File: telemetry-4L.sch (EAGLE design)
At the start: 70 parts, among them SW1 MF-SW-TACT-4.2MM, SW2 PCM12SMTR, U1 ATSAMD21G18A-MUT, U2 SPX3819M5-L-3-0, U3 MCP73831T-2ACI/OT, U4 IRLML6344TRPBF, U5 SIM868, U6 BMP280, U7 MPU-9250, U8 TPS61253YFFR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

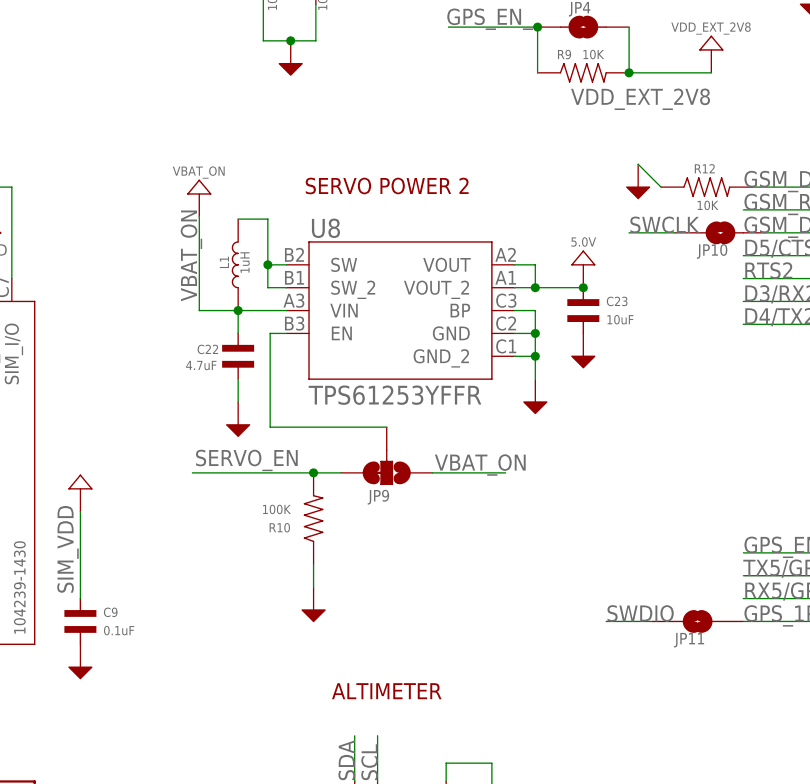
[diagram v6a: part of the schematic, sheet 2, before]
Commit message: Killed "Servo Power 2" components
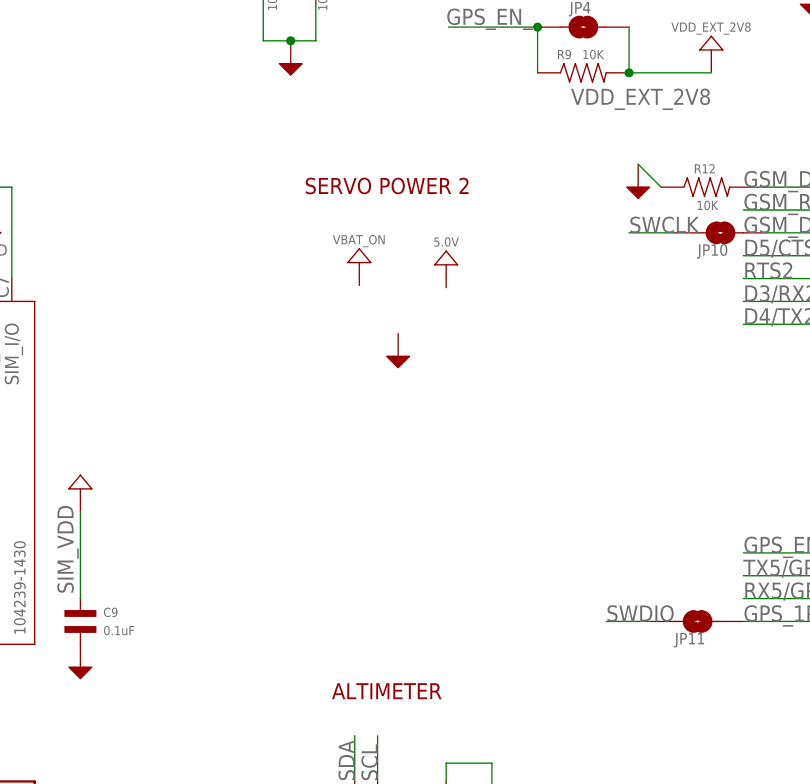
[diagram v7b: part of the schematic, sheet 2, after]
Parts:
- removed C22: 4.7uF, MF_Passives:CAPACITOR_NP_0402
- removed C23: 10uF, MF_Passives:CAPACITOR_NP_0603
- removed JP9: JUMPER-PAD-3-2OF3_NC_BY_TRACE_SMALL, SparkFun-Passives:JUMPER-PAD-3-2OF3_NC_BY_TRACE_SMALL
- removed L1: 1uH, MF_Passives:INDUCTOR_1210
- removed R10: 100K, MF_Passives:RESISTOR_0402
- removed U8: TPS61253YFFR, Custom:TPS61253YFFT
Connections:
- removed net 5VSW: L1.P$2, U8.SW, U8.SW_2
- removed net 5V_EN: JP9.2, U8.EN
- net 5.0V: no longer C23.P$1, U8.VOUT, U8.VOUT_2
- net GND: no longer C22.P$2, C23.P$2, R10.P$1, U8.BP, U8.GND, U8.GND_2
- net SERVO_EN: no longer JP9.3, R10.P$2
- net VBAT_ON: no longer C22.P$1, JP9.1, L1.P$1, U8.VIN
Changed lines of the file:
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@@
 <part name="U$24" library="microbuilder" deviceset="GND" device=""/>
 <part name="U$26" library="microbuilder" deviceset="GND" device=""/>
-<part name="U8" library="Custom" deviceset="TPS61253YFFT" device="" value="TPS61253YFFR"/>
-<part name="L1" library="MF_Passives" deviceset="INDUCTOR" device="_1210" value="1uH">
-<attribute name="MPN" value="1277AS-H-1R0M=P2"/>
-</part>
-<part name="C22" library="MF_Passives" deviceset="CAPACITOR_NP" device="_0402" value="4.7uF">
-<attribute name="MPN" value="GRM155R60J475ME47D"/>
-</part>
-<part name="U$2" library="MF_Aesthetics" deviceset="GND_RAIL" device=""/>
-<part name="C23" library="MF_Passives" deviceset="CAPACITOR_NP" device="_0603" value="10uF">
-<attribute name="MPN" value="GRM188R60J106ME47D"/>
-</part>
-<part name="U$41" library="MF_Aesthetics" deviceset="GND_RAIL" device=""/>
 <part name="U$42" library="MF_Aesthetics" deviceset="POWER_RAIL" device="" value="5.0V"/>
 <part name="U$46" library="MF_Aesthetics" deviceset="GND_RAIL" device=""/>
-<part name="JP9" library="SparkFun-Passives" deviceset="JUMPER-PAD-3-2OF3_NC_BY_TRACE" device="_SMALL">
-<attribute name="POPULATE" value="0"/>
-</part>
 <part name="5.0V_1" library="MF_Aesthetics" deviceset="POWER_RAIL" device="" value="5.0V"/>
 <part name="U$55" library="MF_Aesthetics" deviceset="GND_RAIL" device=""/>
@@
 <attribute name="MPN" value="CL31A107MQHNNNE"/>
 </part>
-<part name="R10" library="MF_Passives" deviceset="RESISTOR" device="_0402" value="100K"/>
-<part name="GND" library="MF_Aesthetics" deviceset="GND_RAIL" device=""/>
 <part name="R11" library="MF_Passives" deviceset="RESISTOR" device="_0402" value="100K"/>
 <part name="R12" library="MF_Passives" deviceset="RESISTOR" device="_0402" value="10K"/>
@@
 <instance part="U$24" gate="G$1" x="69.088" y="17.78"/>
 <instance part="U$26" gate="G$1" x="8.636" y="22.86"/>
-<instance part="U8" gate="A" x="101.6" y="108.204"/>
-<instance part="L1" gate="G$1" x="86.106" y="113.284" smashed="yes" rot="R90">
-<attribute name="NAME" x="85.09" y="114.3" size="1.016" layer="95" font="vector" rot="R270" align="top-left"/>
-<attribute name="VALUE" x="87.376" y="112.268" size="1.016" layer="96" font="vector" rot="R90"/>
-</instance>
-<instance part="C22" gate="G$1" x="86.106" y="103.124" smashed="yes">
-<attribute name="NAME" x="81.534" y="104.394" size="1.016" layer="95" font="vector" align="top-left"/>
-<attribute name="VALUE" x="80.264" y="101.6" size="1.016" layer="96" font="vector"/>
-</instance>
-<instance part="U$2" gate="G$1" x="86.106" y="95.504"/>
-<instance part="C23" gate="G$1" x="124.46" y="108.204"/>
-<instance part="U$41" gate="G$1" x="124.46" y="103.124"/>
-<instance part="U$42" gate="G$1" x="124.46" y="113.284"/>
-<instance part="U$46" gate="G$1" x="119.126" y="98.044"/>
-<instance part="JP9" gate="G$1" x="102.616" y="90.17" smashed="yes" rot="R270">
-<attribute name="NAME" x="100.584" y="86.995" size="1.27" layer="95"/>
-<attribute name="POPULATE" x="102.616" y="90.17" size="1.778" layer="96" rot="R270" display="off"/>
-</instance>
+<instance part="U$42" gate="G$1" x="109.22" y="113.284"/>
+<instance part="U$46" gate="G$1" x="103.886" y="103.124"/>
 <instance part="5.0V_1" gate="G$1" x="91.948" y="157.226"/>
 <instance part="U$55" gate="G$1" x="91.948" y="135.636"/>
-<instance part="U$20" gate="G$1" x="81.788" y="121.158"/>
+<instance part="U$20" gate="G$1" x="99.568" y="113.538"/>
 <instance part="U$34" gate="G$1" x="58.674" y="143.51"/>
 <instance part="U$52" gate="G$1" x="148.844" y="152.4"/>
@@
 <attribute name="VALUE" x="90.424" y="141.478" size="1.016" layer="96" font="vector" rot="R90"/>
 </instance>
-<instance part="R10" gate="G$1" x="94.488" y="85.09" rot="R180"/>
-<instance part="GND" gate="G$1" x="94.488" y="74.93"/>
 <instance part="R11" gate="G$1" x="94.742" y="147.32" smashed="yes">
 <attribute name="NAME" x="91.694" y="150.876" size="1.016" layer="95" font="vector" align="top-left"/>
@@
 </segment>
 <segment>
-<pinref part="C22" gate="G$1" pin="P$2"/>
-<pinref part="U$2" gate="G$1" pin="P$1"/>
-<wire x1="86.106" y1="98.044" x2="86.106" y2="100.584" width="0.1524" layer="91"/>
-</segment>
-<segment>
-<pinref part="C23" gate="G$1" pin="P$2"/>
-<pinref part="U$41" gate="G$1" pin="P$1"/>
-</segment>
-<segment>
-<pinref part="U$46" gate="G$1" pin="P$1"/>
-<pinref part="U8" gate="A" pin="GND"/>
-<wire x1="116.84" y1="105.664" x2="119.126" y2="105.664" width="0.1524" layer="91"/>
-<wire x1="119.126" y1="105.664" x2="119.126" y2="103.124" width="0.1524" layer="91"/>
-<pinref part="U8" gate="A" pin="BP"/>
-<wire x1="119.126" y1="103.124" x2="119.126" y2="100.584" width="0.1524" layer="91"/>
-<wire x1="116.84" y1="108.204" x2="119.126" y2="108.204" width="0.1524" layer="91"/>
-<wire x1="119.126" y1="108.204" x2="119.126" y2="105.664" width="0.1524" layer="91"/>
-<junction x="119.126" y="105.664"/>
-<pinref part="U8" gate="A" pin="GND_2"/>
-<wire x1="116.84" y1="103.124" x2="119.126" y2="103.124" width="0.1524" layer="91"/>
-<junction x="119.126" y="103.124"/>
-</segment>
-<segment>
 <pinref part="U$55" gate="G$1" pin="P$1"/>
 <pinref part="C24" gate="G$1" pin="P$2"/>
@@
 <wire x1="94.742" y1="138.176" x2="91.948" y2="138.176" width="0.1524" layer="91"/>
 <junction x="91.948" y="138.176"/>
-</segment>
-<segment>
-<pinref part="R10" gate="G$1" pin="P$1"/>
-<pinref part="GND" gate="G$1" pin="P$1"/>
-<wire x1="94.488" y1="77.47" x2="94.488" y2="80.01" width="0.1524" layer="91"/>
 </segment>
 <segment>
@@
 </net>
 <net name="VBAT_ON" class="0">
-<segment>
-<pinref part="JP9" gate="G$1" pin="1"/>
-<wire x1="107.696" y1="90.17" x2="115.824" y2="90.17" width="0.1524" layer="91"/>
-<label x="107.95" y="90.424" size="1.778" layer="95"/>
-</segment>
-<segment>
-<wire x1="81.788" y1="108.204" x2="81.788" y2="118.618" width="0.1524" layer="91"/>
-<label x="81.534" y="109.22" size="1.778" layer="95" rot="R90"/>
-<pinref part="L1" gate="G$1" pin="P$1"/>
-<pinref part="C22" gate="G$1" pin="P$1"/>
-<wire x1="86.106" y1="105.664" x2="86.106" y2="108.204" width="0.1524" layer="91"/>
-<wire x1="81.788" y1="108.204" x2="86.106" y2="108.204" width="0.1524" layer="91"/>
-<pinref part="U8" gate="A" pin="VIN"/>
-<wire x1="86.106" y1="108.204" x2="91.44" y2="108.204" width="0.1524" layer="91"/>
-<junction x="86.106" y="108.204"/>
-<pinref part="U$20" gate="G$1" pin="P$1"/>
-</segment>
 <segment>
 <label x="49.53" y="138.684" size="1.778" layer="95"/>
@@
 </segment>
 </net>
-<net name="5VSW" class="0">
-<segment>
-<pinref part="U8" gate="A" pin="SW_2"/>
-<wire x1="91.44" y1="110.744" x2="89.408" y2="110.744" width="0.1524" layer="91"/>
-<wire x1="89.408" y1="110.744" x2="89.408" y2="113.284" width="0.1524" layer="91"/>
-<pinref part="L1" gate="G$1" pin="P$2"/>
-<wire x1="89.408" y1="113.284" x2="89.408" y2="118.364" width="0.1524" layer="91"/>
-<wire x1="89.408" y1="118.364" x2="86.106" y2="118.364" width="0.1524" layer="91"/>
-<pinref part="U8" gate="A" pin="SW"/>
-<wire x1="91.44" y1="113.284" x2="89.408" y2="113.284" width="0.1524" layer="91"/>
-<junction x="89.408" y="113.284"/>
-</segment>
-</net>
 <net name="5.0V" class="0">
-<segment>
-<wire x1="116.84" y1="110.744" x2="119.126" y2="110.744" width="0.1524" layer="91"/>
-<pinref part="U8" gate="A" pin="VOUT_2"/>
-<pinref part="C23" gate="G$1" pin="P$1"/>
-<junction x="124.46" y="110.744"/>
-<pinref part="U$42" gate="G$1" pin="P$1"/>
-<pinref part="U8" gate="A" pin="VOUT"/>
-<wire x1="119.126" y1="110.744" x2="124.46" y2="110.744" width="0.1524" layer="91"/>
-<wire x1="116.84" y1="113.284" x2="119.126" y2="113.284" width="0.1524" layer="91"/>
-<wire x1="119.126" y1="113.284" x2="119.126" y2="110.744" width="0.1524" layer="91"/>
-<junction x="119.126" y="110.744"/>
-</segment>
 <segment>
 <pinref part="5.0V_1" gate="G$1" pin="P$1"/>
@@
 </segment>
 </net>
-<net name="5V_EN" class="0">
-<segment>
-<pinref part="U8" gate="A" pin="EN"/>
-<wire x1="91.44" y1="105.664" x2="89.662" y2="105.664" width="0.1524" layer="91"/>
-<pinref part="JP9" gate="G$1" pin="2"/>
-<wire x1="89.662" y1="105.664" x2="89.662" y2="95.25" width="0.1524" layer="91"/>
-<wire x1="89.662" y1="95.25" x2="102.616" y2="95.25" width="0.1524" layer="91"/>
-</segment>
-</net>
-<net name="SERVO_EN" class="0">
-<segment>
-<pinref part="JP9" gate="G$1" pin="3"/>
-<wire x1="97.536" y1="90.17" x2="94.488" y2="90.17" width="0.1524" layer="91"/>
-<label x="81.28" y="90.932" size="1.778" layer="95"/>
-<pinref part="R10" gate="G$1" pin="P$2"/>
-<wire x1="94.488" y1="90.17" x2="81.026" y2="90.17" width="0.1524" layer="91"/>
-<junction x="94.488" y="90.17"/>
-</segment>
-</net>

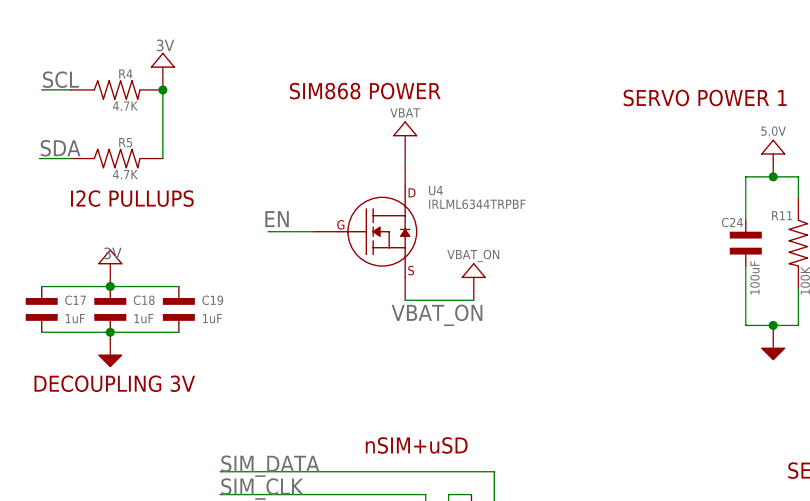
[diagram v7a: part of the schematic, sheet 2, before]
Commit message: Swapped Power MOSFET Source and Drain so it's correct
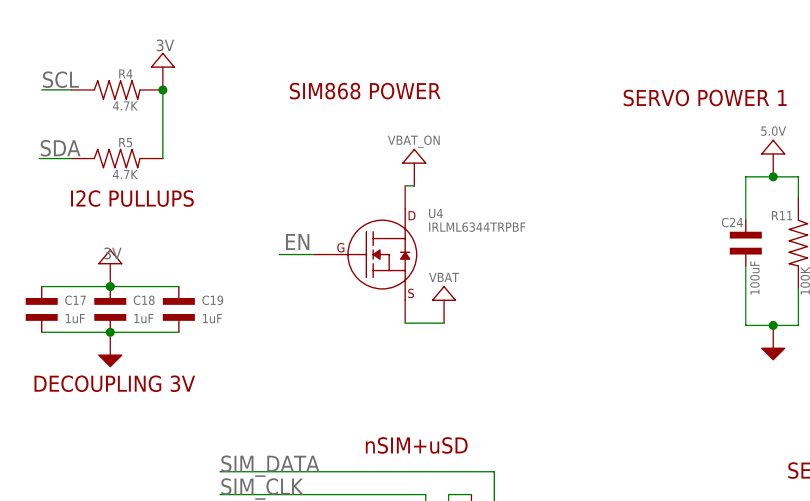
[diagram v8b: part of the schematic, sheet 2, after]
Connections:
- net VBAT: now also U4.SOURCE; no longer U4.DRAIN
- net VBAT_ON: now also U4.DRAIN; no longer U4.SOURCE
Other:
- moved on the sheet: U4
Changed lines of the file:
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@@
 <part name="U$44" library="MF_Aesthetics" deviceset="POWER_RAIL" device="" value="VBAT"/>
 <part name="U4" library="MF_Discrete_Semiconductor" deviceset="N-CHANNEL_FET" device="_SOT-23-3" value="IRLML6344TRPBF"/>
-<part name="VBAT" library="MF_Aesthetics" deviceset="POWER_RAIL" device="" value="VBAT"/>
+<part name="VBAT" library="MF_Aesthetics" deviceset="POWER_RAIL" device="" value="VBAT_ON"/>
 <part name="C19" library="MF_Passives" deviceset="CAPACITOR_NP" device="_0402" value="1uF"/>
 <part name="+3V5" library="MF_Aesthetics" deviceset="POWER_RAIL" device="" value="3V"/>
@@
 <part name="U$55" library="MF_Aesthetics" deviceset="GND_RAIL" device=""/>
 <part name="U$20" library="MF_Aesthetics" deviceset="POWER_RAIL" device="" value="VBAT_ON"/>
-<part name="U$34" library="MF_Aesthetics" deviceset="POWER_RAIL" device="" value="VBAT_ON"/>
+<part name="U$34" library="MF_Aesthetics" deviceset="POWER_RAIL" device="" value="VBAT"/>
 <part name="U$52" library="MF_Aesthetics" deviceset="POWER_RAIL" device="" value="VBAT_ON"/>
 <part name="U$56" library="MF_Aesthetics" deviceset="POWER_RAIL" device="" value="VBAT_ON"/>
@@
 <attribute name="VALUE" x="126.746" y="137.16" size="1.016" layer="96" font="vector" rot="R180"/>
 </instance>
-<instance part="U4" gate="G$1" x="48.514" y="148.59"/>
-<instance part="VBAT" gate="G$1" x="51.054" y="159.258" smashed="yes">
-<attribute name="VALUE" x="51.054" y="161.798" size="1.016" layer="96" font="vector" align="center"/>
+<instance part="U4" gate="G$1" x="48.514" y="146.05"/>
+<instance part="VBAT" gate="G$1" x="52.07" y="156.21" smashed="yes">
+<attribute name="VALUE" x="52.07" y="158.75" size="1.016" layer="96" font="vector" align="center"/>
 </instance>
 <instance part="C19" gate="G$1" x="25.908" y="139.954"/>
@@
 <instance part="U$55" gate="G$1" x="91.948" y="135.636"/>
 <instance part="U$20" gate="G$1" x="99.568" y="113.538"/>
-<instance part="U$34" gate="G$1" x="58.674" y="143.51"/>
+<instance part="U$34" gate="G$1" x="55.372" y="140.97"/>
 <instance part="U$52" gate="G$1" x="148.844" y="152.4"/>
 <instance part="U$56" gate="G$1" x="205.74" y="33.02"/>
@@
 </segment>
 </net>
-<net name="VBAT" class="0">
-<segment>
-<pinref part="U4" gate="G$1" pin="DRAIN"/>
-<pinref part="VBAT" gate="G$1" pin="P$1"/>
-<wire x1="51.054" y1="156.718" x2="51.054" y2="156.21" width="0.1524" layer="91"/>
-</segment>
-</net>
 <net name="GSM_DTR" class="0">
 <segment>
@@
 <segment>
 <pinref part="U4" gate="G$1" pin="GATE"/>
-<wire x1="40.894" y1="148.59" x2="35.814" y2="148.59" width="0.1524" layer="91"/>
-<label x="35.306" y="149.098" size="1.778" layer="95"/>
+<wire x1="40.894" y1="146.05" x2="37.084" y2="146.05" width="0.1524" layer="91"/>
+<label x="37.592" y="146.558" size="1.778" layer="95"/>
 </segment>
 </net>
@@
 </net>
 <net name="VBAT_ON" class="0">
-<segment>
-<label x="49.53" y="138.684" size="1.778" layer="95"/>
-<wire x1="58.674" y1="140.97" x2="51.054" y2="140.97" width="0.1524" layer="91"/>
-<pinref part="U4" gate="G$1" pin="SOURCE"/>
-<pinref part="U$34" gate="G$1" pin="P$1"/>
-</segment>
 <segment>
 <pinref part="U5" gate="G$1" pin="VBAT"/>
@@
 <pinref part="U$56" gate="G$1" pin="P$1"/>
 </segment>
+<segment>
+<pinref part="U4" gate="G$1" pin="DRAIN"/>
+<pinref part="VBAT" gate="G$1" pin="P$1"/>
+<wire x1="52.07" y1="153.67" x2="51.054" y2="153.67" width="0.1524" layer="91"/>
+</segment>
 </net>
 <net name="5.0V" class="0">
@@
 </segment>
 </net>
+<net name="VBAT" class="0">
+<segment>
+<pinref part="U4" gate="G$1" pin="SOURCE"/>
+<pinref part="U$34" gate="G$1" pin="P$1"/>
+<wire x1="55.372" y1="138.43" x2="51.054" y2="138.43" width="0.1524" layer="91"/>
+</segment>
+</net>
